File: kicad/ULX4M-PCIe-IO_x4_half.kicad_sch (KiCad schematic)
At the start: 68 parts, among them J10 FCR684205R, J11 OLED, J12 641737-1, J13 39-30-0060, J14 LM7805_EN, J15 POE, J16 Barrel_Jack, J17 JTAG, J3 SFP+, J4 SFP+, J5 HAT, J6 EXT_USB, J7 Micro_SD_Card_CD, J8 Board_To_Board, J9 FCR684205T, SW1 SW_DIP_x08, SW2 SW_DIP_x08, U10 TPD4E02B04DQA, U11 TPD4E02B04DQA, U12 TPD4E02B04DQA, U13 AT24CS32-SSHM, U14 LM78M05_TO252, U9 TPD4E02B04DQA

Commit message: finalising connections
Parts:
- added AE3: EXT_SERDES_CLK_REF, Connector_Coaxial:SMA_Amphenol_132291-12_Vertical, symbol Device:Antenna_Dipole
- added J18: I2C_to_ID, Connector_PinHeader_2.54mm:PinHeader_2x02_P2.54mm_Vertical, symbol Connector_Generic:Conn_02x02_Odd_Even
- added J19: PCIe_JTAG, Connector_PinHeader_2.54mm:PinHeader_2x04_P2.54mm_Vertical, symbol Connector_Generic:Conn_02x04_Odd_Even
- added J20: PCIe_I2C, Connector_PinHeader_2.54mm:PinHeader_2x02_P2.54mm_Vertical, symbol Connector_Generic:Conn_02x02_Odd_Even
- added J21: PCIe_1X_4X, Connector_PinHeader_2.54mm:PinHeader_2x02_P2.54mm_Vertical, symbol Connector_Generic:Conn_02x02_Odd_Even
- added R23: R220, Resistor_SMD:R_0603_1608Metric, symbol Device:R_Small
- added R24, R27, R28, R29, R46, R47, R48, R49, R50: 4K7, Resistor_SMD:R_0603_1608Metric, symbol Device:R_Small
- added R30, R31, R32, R33, R34, R35, R36, R37, R38, R39, R40, R41, R42, R43, R44, R45: 0R, Resistor_SMD:R_0603_1608Metric, symbol Device:R_Small
- FB1, FB2: footprint (none) -> Inductor_SMD:L_0603_1608Metric
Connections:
- net +12V: now also J15.2 (Pin_2), J15.4 (Pin_4)
- net +3.3V: now also J10.3 (VCC), J11.2 (Pin_2), J9.2 (VCC), R24.1, R27.1, R28.1, R29.1, R46.2, R47.2, R48.2, R49.2, R50.2
- net +5V: now also D1.1 (VDD), D2.1 (VDD), D3.1 (VDD), D4.1 (VDD), D5.1 (VDD), D6.1 (VDD), J6.1 (Pin_1), J6.2 (Pin_2)
- net GND: now also D1.3 (VSS), D2.3 (VSS), D3.3 (VSS), D4.3 (VSS), D5.3 (VSS), D6.3 (VSS), J10.2 (GND), J11.1 (Pin_1), J15.1 (Pin_1), J15.3 (Pin_3), J6.7 (Pin_7), J6.8 (Pin_8), J9.1 (GND), SW1.10, SW1.11, SW1.12, SW1.13, SW1.14, SW1.15, SW1.16, SW1.9, SW2.10, SW2.11, SW2.12, SW2.13, SW2.14, SW2.15, SW2.16, SW2.9, U10.3 (G), U10.8 (G), U9.3 (G), U9.8 (G)
- net GPIO12: now also J19.4 (Pin_4)
- net GPIO16: now also J19.6 (Pin_6)
- net GPIO20: now also J19.2 (Pin_2)
- net GPIO21: now also J19.8 (Pin_8)
- net ID_SC: now also J18.1 (Pin_1)
- net ID_SD: now also J18.3 (Pin_3)
- net PER2_N: now also R35.2, R40.2
- net PER2_P: now also R34.2, R41.2
- net PER3_N: now also R32.2, R38.2
- net PER3_P: now also R33.2, R39.2
- net PET2_N: now also R37.2, R44.2
- net PET2_P: now also R36.2, R45.2
- net PET3_N: now also R30.2, R42.2
- net PET3_P: now also R31.2, R43.2
- net SCL0: now also J18.2 (Pin_2), J20.2 (Pin_2)
- net SDA0: now also J18.4 (Pin_4), J20.4 (Pin_4)
- net SD_CMD: now also R50.1
- net SD_DAT0: now also R46.1
- net SD_DAT1: now also R47.1
- net SD_DAT2: now also R48.1
- net SD_DAT3: now also R49.1
- net SFP0_MOD_ABS: now also R27.2
- net SFP0_RX_N: now also U9.2 (IO2), R36.1
- net SFP0_RX_P: now also U9.1 (IO1), R37.1
- net SFP0_TX_N: now also U9.5 (IO4), R34.1
- net SFP0_TX_P: now also U9.4 (IO3), R35.1
- net SFP1_MOD_ABS: now also R24.2
- net SFP1_RX_N: now also U10.2 (IO2), R32.1
- net SFP1_RX_P: now also U10.1 (IO1), R33.1
- net SFP1_TX_N: now also U10.5 (IO4), R30.1
- net SFP1_TX_P: now also U10.4 (IO3), R31.1
- net SMCLK: now also J20.1 (Pin_1)
- net SMDAT: now also J20.3 (Pin_3)
- net TCK: now also J19.1 (Pin_1)
- net TDI: now also J19.3 (Pin_3)
- net TDO: now also J19.5 (Pin_5)
- net TMS: now also J19.7 (Pin_7)
- net ~{PRSNT1}: now also J21.2 (Pin_2), J21.4 (Pin_4)
- net ~{PRSNT2x1}: now also J21.1 (Pin_1)
- net ~{PRSNT2x4}: now also J21.3 (Pin_3)
- net CAM1_D0_P: now reaches SW2.1
- net CAM1_D0_N: now reaches SW2.2
- net CAM1_D1_P: now reaches SW2.3
- net CAM1_D1_N: now reaches SW2.4
- net CAM0_D0_P: now reaches SW1.1
- net CAM0_D0_N: now reaches SW1.2
- net CAM0_D1_P: now reaches SW1.3
- net CAM0_D1_N: now reaches SW1.4
- net EXT_CLK_REF1_P: now reaches AE1.1
- net EXT_CLK_REF1_N: now reaches AE1.2
- net EXT_CLK_REF2_P: now reaches AE2.1
- net EXT_CLK_REF2_N: now reaches AE2.2
- net OLED_BL: now reaches J3.2 (TX_FAULT), R20.2
- net OLED_BL: now also J11.8 (Pin_8)
- net RS0: now reaches J3.7 (RS0)
- net RS0: now also J4.7 (RS0), R28.2
- net OLED_CS: now reaches J3.8 (RX_LOS), R19.2
- net OLED_CS: now also J11.7 (Pin_7)
- net RS1: now reaches J3.9 (RS1)
- net RS1: now also J4.9 (RS1), R29.2
- net TX_FAULT_1: now reaches J4.2 (TX_FAULT), R22.2
- net RX_LOS_1: now reaches J4.8 (RX_LOS), R21.2
- net USB_ID: now reaches J6.10 (Pin_10)
- net D+: now reaches J6.3 (Pin_3)
- net D+: now also J6.4 (Pin_4)
- net D-: now reaches J6.5 (Pin_5)
- net D-: now also J6.6 (Pin_6)
- net at D2.2 (DOUT): now also D3.4 (DIN)
- net at D2.4 (DIN): now also D1.2 (DOUT)
- net SPDIF_IN: now reaches J9.3 (VIN)
- net at D3.2 (DOUT): now also D4.4 (DIN)
- net at D5.2 (DOUT): now also D6.4 (DIN)
- net at D5.4 (DIN): now also D4.2 (DOUT)
- net OLED_CLK: now reaches J11.3 (Pin_3)
- net OLED_MOSI: now reaches J11.4 (Pin_4)
- net OLED_RES: now reaches J11.5 (Pin_5)
- net OLED_DC: now reaches J11.6 (Pin_6)
- net SPDIF_OUT: now reaches J10.1 (VOUT)
- net at D1.4 (DIN): now also R23.1
- new net EXT__SER_CLK_REF_N: AE3.2
- new net EXT__SER_CLK_REF_P: AE3.1
- new net PER2_PCIe_N: R40.1
- new net PER2_PCIe_P: R41.1
- new net PER3_PCIe_N: R38.1
- new net PER3_PCIe_P: R39.1
- new net PET2_PCIe_N: R44.1
- new net PET2_PCIe_P: R45.1
- new net PET3_PCIe_N: R42.1
- new net PET3_PCIe_P: R43.1
- new net RGB_DATA: R23.2
- no-connect marks 0 -> 1
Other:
- sheet CM4_module ports: added CAM0_C_N, CAM0_C_P, CAM0_D0_N, CAM0_D0_P, CAM0_D1_N, CAM0_D1_P, CAM1_C_N, CAM1_C_P, CAM1_D0_N, CAM1_D0_P, CAM1_D1_N, CAM1_D1_P, Camera_GPIO, DSI0_C_N, DSI0_C_P, DSI0_D0_N, DSI0_D0_P, DSI0_D1_N, DSI0_D1_P, DSI1_C_S1_N, DSI1_C_S1_P, DSI1_D0_S5_N, DSI1_D0_S5_P, DSI1_D1_S7_N, DSI1_D1_S7_P, DSI1_D2_N, DSI1_D2_P, DSI1_D3_N, DSI1_D3_P, ETH0_N, ETH0_P, ETH1_N, ETH1_P, ETH2_N, ETH2_P, ETH3_N, ETH3_P, GPDI1_CEC_PU, GPDI1_HP_PD, GPDI1_SCL_5VPU, GPDI1_SDA_5VPU, PCIe_CLK_N, PCIe_CLK_P, PCIe_CLK_nREQ, PCIe_RX_N, PCIe_RX_P, PCIe_TX_N, PCIe_TX_P, PCIe_nRST, SD_PWR_ON, USB2_N, USB2_P, USB_OTG_ID; removed none
- moved on the sheet: AE1, AE2, C12, C13, C14, C15, D1, D2, D3, D4, D5, D6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

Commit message: Routing PCIe
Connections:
- net SFP0_RX_N: now also R37.1; no longer R36.1
- net SFP0_RX_P: now also R36.1; no longer R37.1
- net SFP0_TX_N: now also R35.1; no longer R34.1
- net SFP0_TX_P: now also R34.1; no longer R35.1
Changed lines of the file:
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@@
     )
   )
-  (global_label "SFP0_RX_N" (shape input) (at -144.526 -78.486 90) (fields_autoplaced)
+  (global_label "SFP0_RX_P" (shape input) (at -144.526 -78.486 90) (fields_autoplaced)
     (effects (font (size 1.27 1.27)) (justify left))
     (property "Intersheetrefs" "${INTERSHEET_REFS}" (at -142.6908 -78.486 90)
@@
     )
   )
-  (global_label "SFP0_TX_P" (shape input) (at -141.478 -78.74 90) (fields_autoplaced)
+  (global_label "SFP0_TX_N" (shape input) (at -141.478 -78.74 90) (fields_autoplaced)
     (effects (font (size 1.27 1.27)) (justify left))
     (property "Intersheetrefs" "${INTERSHEET_REFS}" (at -139.6428 -78.74 90)
@@
     )
   )
-  (global_label "SFP0_TX_N" (shape input) (at -138.938 -78.74 90) (fields_autoplaced)
+  (global_label "SFP0_TX_P" (shape input) (at -138.938 -78.74 90) (fields_autoplaced)
     (effects (font (size 1.27 1.27)) (justify left))
     (property "Intersheetrefs" "${INTERSHEET_REFS}" (at -137.1028 -78.74 90)
@@
     )
   )
-  (global_label "SFP0_RX_P" (shape input) (at -147.066 -78.486 90) (fields_autoplaced)
+  (global_label "SFP0_RX_N" (shape input) (at -147.066 -78.486 90) (fields_autoplaced)
     (effects (font (size 1.27 1.27)) (justify left))
     (property "Intersheetrefs" "${INTERSHEET_REFS}" (at -145.2308 -78.486 90)

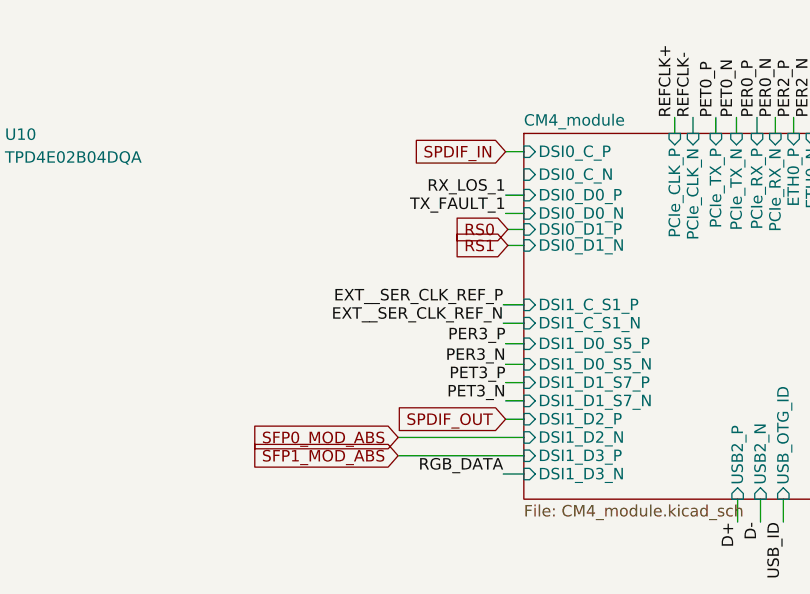
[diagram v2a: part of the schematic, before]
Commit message: Routing GPIOs
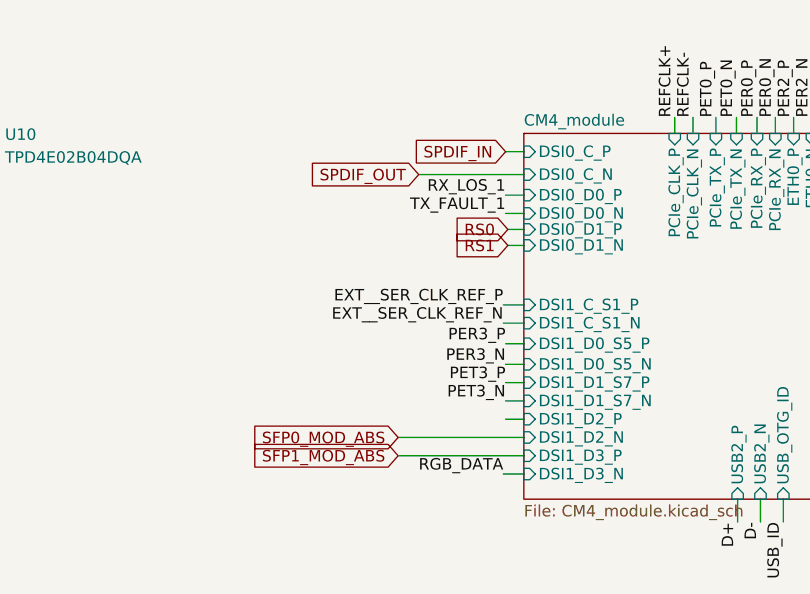
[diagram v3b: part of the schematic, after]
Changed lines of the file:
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@@
+    (stroke (width 0) (type default))
+  )
+  (wire (pts (xy 49.53 -54.61) (xy 61.214 -54.61))
     (stroke (width 0) (type default))
   )
@@
     )
   )
-  (global_label "SPDIF_OUT" (shape input) (at 59.182 -27.432 180) (fields_autoplaced)
-    (effects (font (size 1.27 1.27)) (justify right))
-    (property "Intersheetrefs" "${INTERSHEET_REFS}" (at 47.0501 -27.432 0)
-      (effects (font (size 1.27 1.27)) (justify right) hide)
-    )
+  (global_label "SPDIF_OUT" (shape input) (at 49.53 -54.61 180) (fields_autoplaced)
+    (effects (font (size 1.27 1.27)) (justify right))
+    (property "Intersheetrefs" "${INTERSHEET_REFS}" (at 37.3981 -54.61 0)
+      (effects (font (size 1.27 1.27)) (justify right) hide)
+    )

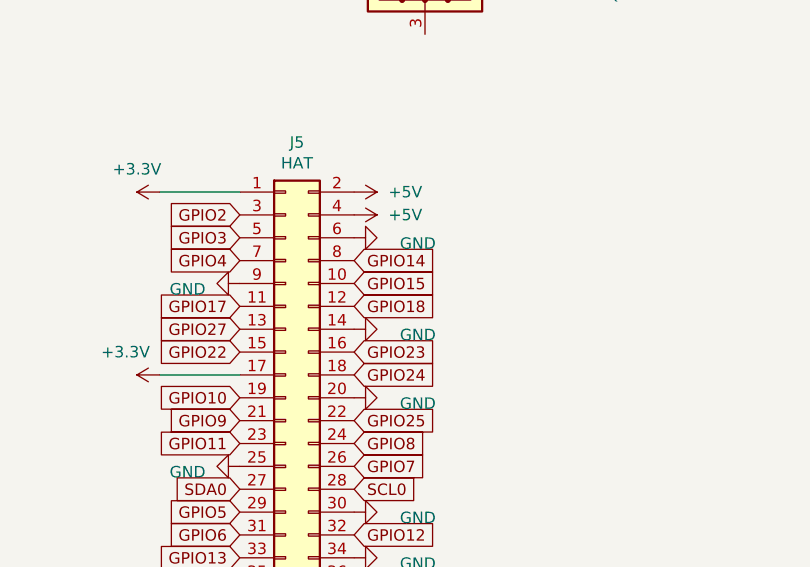
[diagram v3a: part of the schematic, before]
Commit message: Routing all gpio
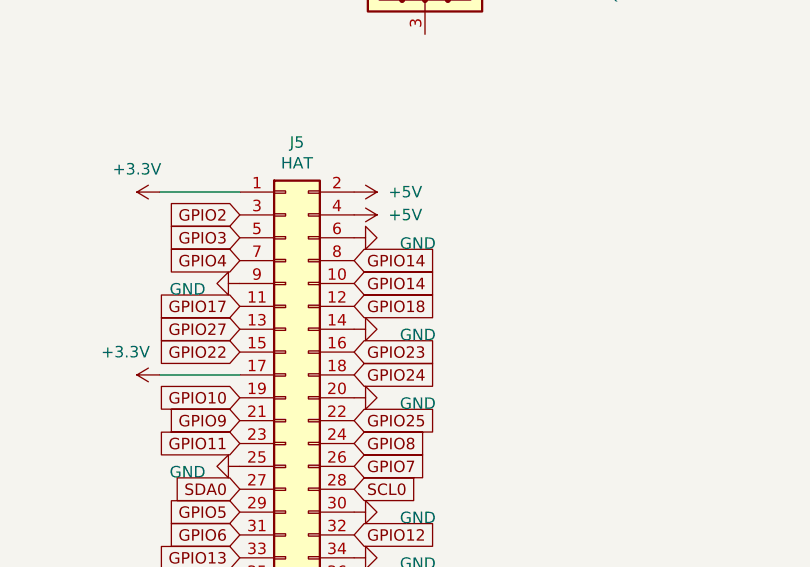
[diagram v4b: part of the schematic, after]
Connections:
- net GPIO15 is gone; now on net GPIO14: J5.10 (Pin_10)
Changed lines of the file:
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@@
     )
   )
-  (global_label "GPIO15" (shape input) (at -48.26 53.34 0) (fields_autoplaced)
+  (global_label "GPIO14" (shape input) (at -48.26 53.34 0) (fields_autoplaced)
     (effects (font (size 1.27 1.27)) (justify left))
     (property "Intersheetrefs" "${INTERSHEET_REFS}" (at -48.26 55.1752 0)

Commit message: Routing
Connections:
- net CAM0_D0_N: now also SW2.1; no longer SW1.2
- net CAM0_D0_P: now also SW2.2; no longer SW1.1
- net CAM0_D1_N: now also SW1.5; no longer SW1.4
- net CAM0_D1_P: now also SW1.6; no longer SW1.3
- net CAM1_D0_N: now also SW2.4; no longer SW2.2
- net CAM1_D0_P: now also SW2.3; no longer SW2.1
- net CAM1_D1_N: now also SW1.2; no longer SW2.4
- net CAM1_D1_P: now also SW1.1; no longer SW2.3
- net GND: now also J7.11 (CD), J7.9 (SHIELD)
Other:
- moved on the sheet: SW1, SW2
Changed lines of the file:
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@@
     (stroke (width 0) (type default))
   )
-  (wire (pts (xy 225.044 -73.66) (xy 229.362 -73.66))
+  (wire (pts (xy 226.06 -73.66) (xy 229.362 -73.66))
     (stroke (width 0) (type default))
   )
@@
     (stroke (width 0) (type default))
   )
-  (wire (pts (xy 225.044 -76.2) (xy 229.362 -76.2))
+  (wire (pts (xy 226.06 -76.2) (xy 229.362 -76.2))
     (stroke (width 0) (type default))
   )
@@
     (stroke (width 0) (type default))
   )
-  (wire (pts (xy 225.552 -36.83) (xy 229.362 -36.83))
+  (wire (pts (xy 226.06 -36.83) (xy 229.362 -36.83))
     (stroke (width 0) (type default))
   )
@@
     (stroke (width 0) (type default))
   )
-  (wire (pts (xy 225.552 -39.37) (xy 229.362 -39.37))
+  (wire (pts (xy 226.06 -39.37) (xy 229.362 -39.37))
     (stroke (width 0) (type default))
   )
-  (wire (pts (xy 225.552 -34.29) (xy 229.362 -34.29))
+  (wire (pts (xy 226.06 -34.29) (xy 229.362 -34.29))
     (stroke (width 0) (type default))
   )
@@
     (stroke (width 0) (type default))
   )
-  (wire (pts (xy 225.552 -46.99) (xy 229.362 -46.99))
+  (wire (pts (xy 226.06 -46.99) (xy 229.362 -46.99))
     (stroke (width 0) (type default))
   )
@@
     (stroke (width 0) (type default))
   )
-  (wire (pts (xy 225.552 -52.07) (xy 229.362 -52.07))
+  (wire (pts (xy 226.06 -52.07) (xy 229.362 -52.07))
     (stroke (width 0) (type default))
   )
@@
     (stroke (width 0) (type default))
   )
-  (wire (pts (xy 225.044 -68.58) (xy 229.362 -68.58))
+  (wire (pts (xy 226.06 -68.58) (xy 229.362 -68.58))
     (stroke (width 0) (type default))
   )
@@
     (stroke (width 0) (type default))
   )
-  (wire (pts (xy 225.044 -66.04) (xy 229.362 -66.04))
+  (wire (pts (xy 226.06 -66.04) (xy 229.362 -66.04))
     (stroke (width 0) (type default))
   )
@@
     (stroke (width 0) (type default))
   )
-  (wire (pts (xy 225.044 -63.5) (xy 229.362 -63.5))
+  (wire (pts (xy 226.06 -63.5) (xy 229.362 -63.5))
     (stroke (width 0) (type default))
   )
@@
     (stroke (width 0) (type default))
   )
-  (wire (pts (xy 225.044 -81.28) (xy 229.362 -81.28))
+  (wire (pts (xy 226.06 -81.28) (xy 229.362 -81.28))
     (stroke (width 0) (type default))
   )
@@
     (stroke (width 0) (type default))
   )
-  (wire (pts (xy 225.552 -44.45) (xy 229.362 -44.45))
+  (wire (pts (xy 226.06 -44.45) (xy 229.362 -44.45))
     (stroke (width 0) (type default))
   )
@@
     (stroke (width 0) (type default))
   )
-  (wire (pts (xy 225.044 -78.74) (xy 229.362 -78.74))
+  (wire (pts (xy 226.06 -78.74) (xy 229.362 -78.74))
     (stroke (width 0) (type default))
   )
@@
     (stroke (width 0) (type default))
   )
-  (wire (pts (xy 225.552 -41.91) (xy 229.362 -41.91))
+  (wire (pts (xy 226.06 -41.91) (xy 229.362 -41.91))
     (stroke (width 0) (type default))
   )
@@
     (stroke (width 0) (type default))
   )
-  (wire (pts (xy 225.044 -71.12) (xy 229.362 -71.12))
+  (wire (pts (xy 226.06 -71.12) (xy 229.362 -71.12))
     (stroke (width 0) (type default))
   )
@@
     (stroke (width 0) (type default))
   )
-  (wire (pts (xy 225.552 -49.53) (xy 229.362 -49.53))
+  (wire (pts (xy 226.06 -49.53) (xy 229.362 -49.53))
     (stroke (width 0) (type default))
   )
@@
     (effects (font (size 1.27 1.27)) (justify left bottom))
   )
-  (label "CAM1_D1_N" (at 210.312 -44.45 180) (fields_autoplaced)
+  (label "CAM1_D1_N" (at 210.82 -78.74 180) (fields_autoplaced)
     (effects (font (size 1.27 1.27)) (justify right bottom))
   )
@@
     (effects (font (size 1.27 1.27)) (justify right bottom))
   )
-  (label "CAM1_D1_P" (at 210.312 -46.99 180) (fields_autoplaced)
+  (label "CAM1_D1_P" (at 210.82 -81.28 180) (fields_autoplaced)
     (effects (font (size 1.27 1.27)) (justify right bottom))
   )
@@
     (effects (font (size 1.27 1.27)) (justify right bottom))
   )
-  (label "CAM0_D1_N" (at 209.804 -73.66 180) (fields_autoplaced)
+  (label "CAM0_D1_N" (at 210.82 -71.12 180) (fields_autoplaced)
     (effects (font (size 1.27 1.27)) (justify right bottom))
   )
@@
     (effects (font (size 1.27 1.27)) (justify right bottom))
   )
-  (label "CAM1_D0_N" (at 210.312 -49.53 180) (fields_autoplaced)
+  (label "CAM1_D0_N" (at 210.82 -44.45 180) (fields_autoplaced)
     (effects (font (size 1.27 1.27)) (justify right bottom))
   )
@@
     (effects (font (size 1.27 1.27)) (justify left bottom))
   )
-  (label "CAM0_D1_P" (at 209.804 -76.2 180) (fields_autoplaced)
+  (label "CAM0_D1_P" (at 210.82 -68.58 180) (fields_autoplaced)
     (effects (font (size 1.27 1.27)) (justify right bottom))
   )
@@
     (effects (font (size 1.27 1.27)) (justify right bottom))
   )
-  (label "CAM0_D0_P" (at 209.804 -81.28 180) (fields_autoplaced)
+  (label "CAM0_D0_P" (at 210.82 -49.53 180) (fields_autoplaced)
     (effects (font (size 1.27 1.27)) (justify right bottom))
   )
@@
     (effects (font (size 1.27 1.27)) (justify left bottom))
   )
-  (label "CAM0_D0_N" (at 209.804 -78.74 180) (fields_autoplaced)
+  (label "CAM0_D0_N" (at 210.82 -52.07 180) (fields_autoplaced)
     (effects (font (size 1.27 1.27)) (justify right bottom))
   )
@@
     (effects (font (size 1.27 1.27)) (justify right bottom))
   )
-  (label "CAM1_D0_P" (at 210.312 -52.07 180) (fields_autoplaced)
+  (label "CAM1_D0_P" (at 210.82 -46.99 180) (fields_autoplaced)
     (effects (font (size 1.27 1.27)) (justify right bottom))
   )
@@
     )
   )
-  (symbol (lib_id "Switch:SW_DIP_x08") (at 217.932 -41.91 0) (unit 1)
+  (symbol (lib_id "Switch:SW_DIP_x08") (at 218.44 -41.91 0) (unit 1)
     (in_bom yes) (on_board yes) (dnp no)
-    (property "Reference" "SW2" (at 217.932 -58.8518 0)
+    (property "Reference" "SW2" (at 218.44 -58.8518 0)
       (effects (font (size 1.27 1.27)))
     )
-    (property "Value" "SW_DIP_x08" (at 217.932 -56.5404 0)
+    (property "Value" "SW_DIP_x08" (at 218.44 -56.5404 0)
       (effects (font (size 1.27 1.27)))
     )
-    (property "Footprint" "Button_Switch_SMD:SW_DIP_SPSTx08_Slide_Omron_A6S-810x_W8.9mm_P2.54mm" (at 217.932 -41.91 0)
+    (property "Footprint" "Button_Switch_SMD:SW_DIP_SPSTx08_Slide_Omron_A6S-810x_W8.9mm_P2.54mm" (at 218.44 -41.91 0)
       (effects (font (size 1.27 1.27)) hide)
     )
-    (property "Datasheet" "~" (at 217.932 -41.91 0)
+    (property "Datasheet" "~" (at 218.44 -41.91 0)
       (effects (font (size 1.27 1.27)) hide)
     )
@@
     )
   )
-  (symbol (lib_id "Switch:SW_DIP_x08") (at 217.424 -71.12 0) (unit 1)
+  (symbol (lib_id "Switch:SW_DIP_x08") (at 218.44 -71.12 0) (unit 1)
     (in_bom yes) (on_board yes) (dnp no)
-    (property "Reference" "SW1" (at 217.424 -88.0618 0)
+    (property "Reference" "SW1" (at 218.44 -88.0618 0)
       (effects (font (size 1.27 1.27)))
     )
-    (property "Value" "SW_DIP_x08" (at 217.424 -85.7504 0)
+    (property "Value" "SW_DIP_x08" (at 218.44 -85.7504 0)
       (effects (font (size 1.27 1.27)))
     )
-    (property "Footprint" "Button_Switch_SMD:SW_DIP_SPSTx08_Slide_Omron_A6S-810x_W8.9mm_P2.54mm" (at 217.424 -71.12 0)
+    (property "Footprint" "Button_Switch_SMD:SW_DIP_SPSTx08_Slide_Omron_A6S-810x_W8.9mm_P2.54mm" (at 218.44 -71.12 0)
       (effects (font (size 1.27 1.27)) hide)
     )
-    (property "Datasheet" "~" (at 217.424 -71.12 0)
+    (property "Datasheet" "~" (at 218.44 -71.12 0)
       (effects (font (size 1.27 1.27)) hide)
     )
@@
     )
   )
+  (symbol (lib_id "power:GND") (at 21.59 195.58 0) (unit 1)
+    (in_bom yes) (on_board yes) (dnp no) (fields_autoplaced)
+    (property "Reference" "#PWR0154" (at 21.59 201.93 0)
+      (effects (font (size 1.27 1.27)) hide)
+    )
+    (property "Value" "GND" (at 21.59 200.66 0)
+      (effects (font (size 1.27 1.27)))
+    )
+    (property "Footprint" "" (at 21.59 195.58 0)
+      (effects (font (size 1.27 1.27)) hide)
+    )
+    (property "Datasheet" "" (at 21.59 195.58 0)
+      (effects (font (size 1.27 1.27)) hide)
+    )
+    (pin "1")
+    (instances
+      (project "ULX4M-PCIe-IO_x4_half"
+        (path "/e227bafe-08dc-4b2a-9df8-340d24e6faf1"
+          (reference "#PWR0154") (unit 1) (value "GND") (footprint "")
+        )
+      )
+    )
+  )
   (symbol (lib_id "Connector_Generic:Conn_02x03_Odd_Even") (at 171.45 124.46 0) (unit 1)
     (in_bom yes) (on_board yes) (dnp no) (fields_autoplaced)
@@
         )
       )
+    )
+  )
+  (symbol (lib_id "power:GND") (at 15.24 176.53 270) (unit 1)
+    (in_bom yes) (on_board yes) (dnp no) (fields_autoplaced)
+    (property "Reference" "#PWR0154" (at 8.89 176.53 0)
+      (effects (font (size 1.27 1.27)) hide)
+    )
+    (property "Value" "GND" (at 11.43 177.165 90)
+      (effects (font (size 1.27 1.27)) (justify right))
+    )
+    (property "Footprint" "" (at 15.24 176.53 0)
+      (effects (font (size 1.27 1.27)) hide)
+    )
+    (property "Datasheet" "" (at 15.24 176.53 0)
+      (effects (font (size 1.27 1.27)) hide)
+    )
+    (pin "1")
+    (instances
+      (project "ULX4M-PCIe-IO_x4_half"
+        (path "/e227bafe-08dc-4b2a-9df8-340d24e6faf1"
+          (reference "#PWR0154") (unit 1) (value "GND") (footprint "")
+        )
+      )
